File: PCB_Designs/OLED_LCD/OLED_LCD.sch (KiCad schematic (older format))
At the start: 25 parts, among them P1 CONN_01X10, P2 CONN_01X20, SW1 Rotary_Encoder_Switch, U1 MCP23017, U2 MCP23017, U3 CHERRY-MX

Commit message: s¨å
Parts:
- removed 0.1k1: 100, Resistors_SMD:R_0603_HandSoldering, symbol R
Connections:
- net LED+ is gone; now on net LCD_BACKLIGHT: P2.19 (P19)
- net RST#: no longer U1.18 (~RESET), U2.18 (~RESET)
- no-connect marks 19 -> 21
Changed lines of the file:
@@
 Text Label 4550 4350 0    60   ~ 0
 GND
-Text Label 5050 2550 0    60   ~ 0
-RST#
 Wire Wire Line
 	5050 3950 5150 3950
@@
 Text Label 7300 4000 2    60   ~ 0
 VEE
-Text Label 7300 4100 2    60   ~ 0
-LED+
 Text Label 7300 4200 2    60   ~ 0
 LED-
-$Comp
-L R 0.1k1
-U 1 1 58950747
-P 6000 4250
-F 0 "0.1k1" V 6080 4250 50  0000 C CNN
-F 1 "100" V 6000 4250 50  0000 C CNN
-F 2 "Resistors_SMD:R_0603_HandSoldering" V 5930 4250 50  0001 C CNN
-F 3 "" H 6000 4250 50  0000 C CNN
-	1    6000 4250
-	1    0    0    -1
-$EndComp
-Wire Wire Line
-	6000 4550 6000 4400
-Text Label 6000 4100 0    60   ~ 0
-LED+
-Text Label 6000 4550 0    60   ~ 0
-VCC5
 $Comp
 L GND #PWR03
@@
 Text Label 2500 3750 0    60   ~ 0
 SDA#
-Text Label 2500 2550 0    60   ~ 0
-RST#
 Text Label 2500 3050 0    60   ~ 0
 INTA
@@
 	1    0    0    -1
 $EndComp
+Text Label 7300 4100 2    60   ~ 0
+LCD_BACKLIGHT
+NoConn ~ 5050 2550
+NoConn ~ 2500 2550
 $EndSCHEMATC

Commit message: LCD123
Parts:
- P1: footprint Connectors:IDC_Header_Straight_10pins -> Connectors_Multicomp:Multicomp_MC9A22-1034_2x05x2.54mm_Angled
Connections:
- net GND: now also P1.4 (P4)
- net INTA: now also P1.10 (P10)
- net SCL#: now also P1.8 (P8)
- net SDA#: now also P1.6 (P6)
- net INTB: no longer names the net of U1.19 (INTB)
- no-connect marks 21 -> 19
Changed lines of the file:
@@
 Text Label 2500 3050 0    60   ~ 0
 INTA
-Text Label 2500 2950 0    60   ~ 0
-INTB
 Text Label 2000 4350 0    60   ~ 0
 GND
@@
 F 0 "P1" H 6000 1850 50  0000 C CNN
 F 1 "CONN_01X10" V 6100 1300 50  0000 C CNN
-F 2 "Connectors:IDC_Header_Straight_10pins" H 6000 1300 50  0001 C CNN
+F 2 "Connectors_Multicomp:Multicomp_MC9A22-1034_2x05x2.54mm_Angled" H 6000 1300 50  0001 C CNN
 F 3 "" H 6000 1300 50  0000 C CNN
 	1    6000 1300
@@
 Text Label 5800 1250 2    60   ~ 0
 SDA#
-Text Label 4850 1150 2    60   ~ 0
-RST#
 Text Label 6550 3150 2    60   ~ 0
 VCC5DISP
@@
 	5050 3750 5500 3750
 Connection ~ 2000 2350
-NoConn ~ 5800 1750
 NoConn ~ 1500 3950
 NoConn ~ 1500 4050
 NoConn ~ 1500 4150
 Connection ~ 2500 3050
-Connection ~ 2500 2950
 Text Label 5800 1650 2    60   ~ 0
 INTA
@@
 Text Label 5800 950  2    60   ~ 0
 LCD_BACKLIGHT
-NoConn ~ 5800 1150
-NoConn ~ 5800 1350
-NoConn ~ 5800 1550
 Text Label 4200 1450 2    60   ~ 0
 VCC5
@@
 NoConn ~ 5050 2550
 NoConn ~ 2500 2550
+NoConn ~ 2500 2950
+NoConn ~ 2800 2950
+Wire Wire Line
+	5800 1050 5800 1150
+Wire Wire Line
+	5800 1250 5800 1350
+Wire Wire Line
+	5800 1450 5800 1550
+Wire Wire Line
+	5800 1650 5800 1750
 $EndSCHEMATC

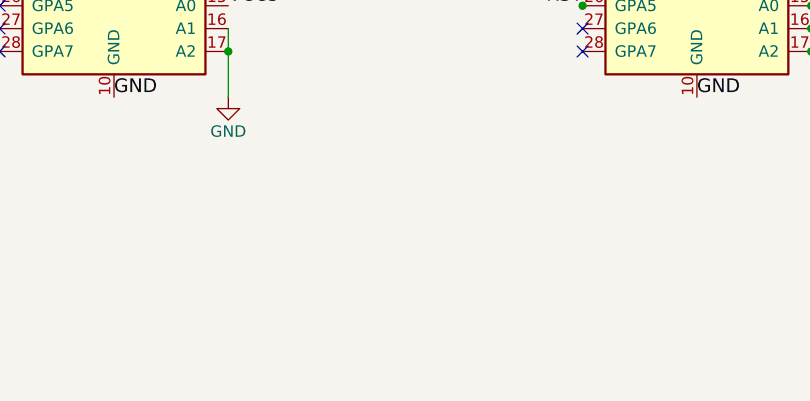
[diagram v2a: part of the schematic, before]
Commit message: Completed OLED_LCD_PCB v1.1
* Added Mountingholes.
* Added "Fatpads" for vias (were on some but not all earlier)
* Added bottom ground (Or etching will be a bitch)
* Added Edge cuts (105x65mm)
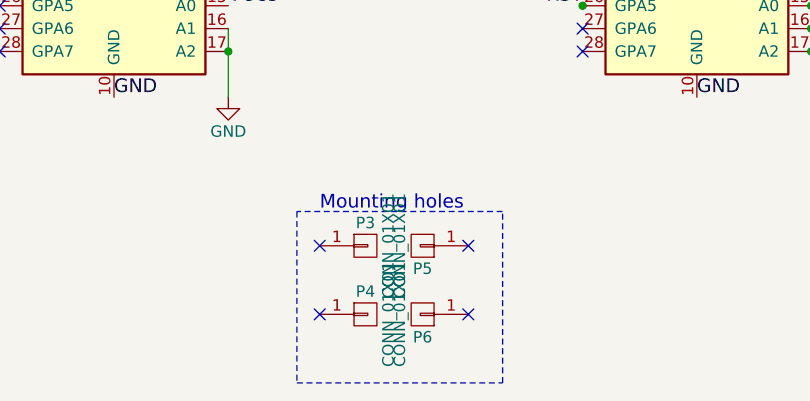
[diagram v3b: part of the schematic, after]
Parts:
- added P3, P4, P5, P6: CONN_01X01, Mounting_Holes:MountingHole_2.2mm_M2_DIN965_Pad, symbol CONN_01X01
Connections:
- no-connect marks 19 -> 23
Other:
- note added: "Mounting holes"
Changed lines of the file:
@@
 Wire Wire Line
 	5800 1650 5800 1750
+$Comp
+L CONN_01X01 P3
+U 1 1 58A4BCD7
+P 3100 5000
+F 0 "P3" H 3100 5100 50  0000 C CNN
+F 1 "CONN_01X01" V 3200 5000 50  0000 C CNN
+F 2 "Mounting_Holes:MountingHole_2.2mm_M2_DIN965_Pad" H 3100 5000 50  0001 C CNN
+F 3 "" H 3100 5000 50  0001 C CNN
+	1    3100 5000
+	1    0    0    -1
+$EndComp
+$Comp
+L CONN_01X01 P5
+U 1 1 58A4C0C0
+P 3350 5000
+F 0 "P5" H 3350 5100 50  0000 C CNN
+F 1 "CONN_01X01" V 3450 5000 50  0000 C CNN
+F 2 "Mounting_Holes:MountingHole_2.2mm_M2_DIN965_Pad" H 3350 5000 50  0001 C CNN
+F 3 "" H 3350 5000 50  0001 C CNN
+	1    3350 5000
+	-1   0    0    1
+$EndComp
+$Comp
+L CONN_01X01 P4
+U 1 1 58A4C14F
+P 3100 5300
+F 0 "P4" H 3100 5400 50  0000 C CNN
+F 1 "CONN_01X01" V 3200 5300 50  0000 C CNN
+F 2 "Mounting_Holes:MountingHole_2.2mm_M2_DIN965_Pad" H 3100 5300 50  0001 C CNN
+F 3 "" H 3100 5300 50  0001 C CNN
+	1    3100 5300
+	1    0    0    -1
+$EndComp
+$Comp
+L CONN_01X01 P6
+U 1 1 58A4C1C4
+P 3350 5300
+F 0 "P6" H 3350 5400 50  0000 C CNN
+F 1 "CONN_01X01" V 3450 5300 50  0000 C CNN
+F 2 "Mounting_Holes:MountingHole_2.2mm_M2_DIN965_Pad" H 3350 5300 50  0001 C CNN
+F 3 "" H 3350 5300 50  0001 C CNN
+	1    3350 5300
+	-1   0    0    1
+$EndComp
+Text Notes 2900 4850 0    60   ~ 0
+Mounting holes
+NoConn ~ 2900 5000
+NoConn ~ 2900 5300
+NoConn ~ 3550 5000
+NoConn ~ 3550 5300
+Wire Notes Line
+	3700 5600 3700 4850
+Wire Notes Line
+	3700 4850 2800 4850
+Wire Notes Line
+	2800 4850 2800 5600
+Wire Notes Line
+	2800 5600 3700 5600
 $EndSCHEMATC

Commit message: hej
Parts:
- removed 10k8: 10k, Potentiometers:Potentiometer_Trimmer-EVM3E, symbol POT
- removed P2: CONN_01X20, Pin_Headers:Pin_Header_Straight_1x20_Pitch2.54mm, symbol CONN_01X20
- added P2: CONN_01X16, Pin_Headers:Pin_Header_Straight_1x16_Pitch2.54mm, symbol CONN_01X16
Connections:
- net D0: now also P2.7 (P7)
- net D1: now also P2.8 (P8)
- net D2: now also P2.9 (P9)
- net D3: now also P2.10 (P10)
- net D4: now also P2.11 (P11)
- net D5: now also P2.12 (P12)
- net D6: now also P2.13 (P13)
- net D7: now also P2.14 (P14)
- net E: now also P2.6 (P6)
- net GND: now also P2.1 (P1), P2.16 (P16)
- net LCD_BACKLIGHT: now also P2.15 (P15)
- net RS: now also P2.4 (P4)
- net RW: now also P2.5 (P5)
- net VCC5: now also P2.2 (P2)
- net CS1: no longer names the net of U2.21 (GPA0)
- net CS2: no longer names the net of U2.22 (GPA1)
- net RST: no longer names the net of U2.26 (GPA5)
- no-connect marks 23 -> 27
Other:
- moved on the sheet: 100n3
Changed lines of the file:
@@
 Text Label 4050 3250 2    60   ~ 0
 D7
-$Comp
-L CONN_01X20 P2
-U 1 1 5894F9E5
-P 7500 3250
-F 0 "P2" H 7500 4300 50  0000 C CNN
-F 1 "CONN_01X20" V 7600 3250 50  0000 C CNN
-F 2 "Pin_Headers:Pin_Header_Straight_1x20_Pitch2.54mm" H 7500 3250 50  0001 C CNN
-F 3 "" H 7500 3250 50  0000 C CNN
-	1    7500 3250
-	1    0    0    -1
-$EndComp
 Text Label 4550 4350 0    60   ~ 0
 GND
@@
 L GND #PWR02
 U 1 1 5894FCE6
-P 6550 3800
-F 0 "#PWR02" H 6550 3550 50  0001 C CNN
-F 1 "GND" H 6550 3650 50  0000 C CNN
-F 2 "" H 6550 3800 50  0000 C CNN
-F 3 "" H 6550 3800 50  0000 C CNN
-	1    6550 3800
+P 6300 3250
+F 0 "#PWR02" H 6300 3000 50  0001 C CNN
+F 1 "GND" H 6300 3100 50  0000 C CNN
+F 2 "" H 6300 3250 50  0000 C CNN
+F 3 "" H 6300 3250 50  0000 C CNN
+	1    6300 3250
 	1    0    0    -1
 $EndComp
@@
 L C 100n3
 U 1 1 5894FD05
-P 6550 3500
-F 0 "100n3" H 6575 3600 50  0000 L CNN
-F 1 "100n" H 6575 3400 50  0000 L CNN
-F 2 "Capacitors_SMD:C_0603_HandSoldering" H 6588 3350 50  0001 C CNN
-F 3 "" H 6550 3500 50  0000 C CNN
-	1    6550 3500
-	1    0    0    -1
-$EndComp
-Wire Wire Line
-	6550 3800 6550 3650
-Text Label 6550 3350 0    60   ~ 0
+P 6300 2950
+F 0 "100n3" H 6325 3050 50  0000 L CNN
+F 1 "100n" H 6325 2850 50  0000 L CNN
+F 2 "Capacitors_SMD:C_0603_HandSoldering" H 6338 2800 50  0001 C CNN
+F 3 "" H 6300 2950 50  0000 C CNN
+	1    6300 2950
+	1    0    0    -1
+$EndComp
+Wire Wire Line
+	6300 3250 6300 3100
+Text Label 6300 2800 0    60   ~ 0
 VCC5
 Text Label 5050 3650 0    60   ~ 0
@@
 Text Label 5050 3750 0    60   ~ 0
 SDA#
-Text Label 4050 3450 2    60   ~ 0
-CS1
-Text Label 4050 3550 2    60   ~ 0
-CS2
 Text Label 4050 3650 2    60   ~ 0
 RS
@@
 Text Label 4050 3850 2    60   ~ 0
 E
-Text Label 4050 3950 2    60   ~ 0
-RST
 Text Label 7300 2300 2    60   ~ 0
-CS1
+GND
 Text Label 7300 2400 2    60   ~ 0
-CS2
-Text Label 7300 2500 2    60   ~ 0
-GND
+VCC5DISP
 Text Label 7300 2600 2    60   ~ 0
-VCC5DISP
+RS
 Text Label 7300 2700 2    60   ~ 0
-V0
+RW
 Text Label 7300 2800 2    60   ~ 0
-RS
+E
 Text Label 7300 2900 2    60   ~ 0
-RW
+D0
 Text Label 7300 3000 2    60   ~ 0
-E
+D1
 Text Label 7300 3100 2    60   ~ 0
-D0
+D2
 Text Label 7300 3200 2    60   ~ 0
-D1
+D3
 Text Label 7300 3300 2    60   ~ 0
-D2
+D4
 Text Label 7300 3400 2    60   ~ 0
-D3
+D5
 Text Label 7300 3500 2    60   ~ 0
-D4
+D6
 Text Label 7300 3600 2    60   ~ 0
-D5
-Text Label 7300 3700 2    60   ~ 0
-D6
+D7
 Text Label 7300 3800 2    60   ~ 0
-D7
-Text Label 7300 3900 2    60   ~ 0
-RST
-Text Label 7300 4000 2    60   ~ 0
-VEE
-Text Label 7300 4200 2    60   ~ 0
 LED-
 $Comp
@@
 L GND #PWR04
 U 1 1 58950905
-P 7150 4350
-F 0 "#PWR04" H 7150 4100 50  0001 C CNN
-F 1 "GND" H 7150 4200 50  0000 C CNN
-F 2 "" H 7150 4350 50  0000 C CNN
-F 3 "" H 7150 4350 50  0000 C CNN
-	1    7150 4350
-	1    0    0    -1
-$EndComp
-Wire Wire Line
-	7300 4200 7150 4200
-Wire Wire Line
-	7150 4200 7150 4350
-$Comp
-L POT 10k8
-U 1 1 58950B2C
-P 6150 2600
-F 0 "10k8" V 5975 2600 50  0000 C CNN
-F 1 "10k" V 6050 2600 50  0000 C CNN
-F 2 "Potentiometers:Potentiometer_Trimmer-EVM3E" H 6150 2600 50  0001 C CNN
-F 3 "" H 6150 2600 50  0000 C CNN
-	1    6150 2600
-	0    1    1    0
-$EndComp
-Text Label 6300 2600 0    60   ~ 0
-VEE
-Text Label 6000 2600 2    60   ~ 0
-GND
-Text Label 6150 2750 0    60   ~ 0
-V0
+P 7100 3900
+F 0 "#PWR04" H 7100 3650 50  0001 C CNN
+F 1 "GND" H 7100 3750 50  0000 C CNN
+F 2 "" H 7100 3900 50  0000 C CNN
+F 3 "" H 7100 3900 50  0000 C CNN
+	1    7100 3900
+	1    0    0    -1
+$EndComp
 $Comp
 L MCP23017 U1
@@
 Wire Wire Line
 	2700 1100 2700 1250
-Connection ~ 6550 3650
+Connection ~ 6300 3100
 Connection ~ 5050 3950
 Connection ~ 5050 4050
@@
 Connection ~ 4050 2650
 Connection ~ 4050 2550
-Connection ~ 4050 3450
-Connection ~ 4050 3550
 Connection ~ 4050 3650
 Connection ~ 4050 3750
 Connection ~ 4050 3850
-Connection ~ 4050 3950
 NoConn ~ 4050 4050
 NoConn ~ 4050 4150
@@
 Text Label 5800 1250 2    60   ~ 0
 SDA#
-Text Label 6550 3150 2    60   ~ 0
+Text Label 6300 2600 2    60   ~ 0
 VCC5DISP
 Wire Wire Line
-	6550 3150 6550 3350
-Connection ~ 6550 3350
+	6300 2600 6300 2800
+Connection ~ 6300 2800
 $Comp
 L R 10k6
@@
 	1    0    0    -1
 $EndComp
-Text Label 7300 4100 2    60   ~ 0
+Text Label 7300 3700 2    60   ~ 0
 LCD_BACKLIGHT
 NoConn ~ 5050 2550
@@
 Wire Notes Line
 	2800 5600 3700 5600
+NoConn ~ 7300 2500
+Wire Wire Line
+	7100 3900 7100 3800
+Wire Wire Line
+	7100 3800 7300 3800
+Connection ~ 7300 3800
+$Comp
+L CONN_01X16 P2
+U 1 1 58B162AE
+P 7500 3050
+F 0 "P2" H 7500 3900 50  0000 C CNN
+F 1 "CONN_01X16" V 7600 3050 50  0000 C CNN
+F 2 "Pin_Headers:Pin_Header_Straight_1x16_Pitch2.54mm" H 7500 3050 50  0001 C CNN
+F 3 "" H 7500 3050 50  0000 C CNN
+	1    7500 3050
+	1    0    0    -1
+$EndComp
+NoConn ~ 4050 3450
+NoConn ~ 4050 3550
+NoConn ~ 4050 3950
 $EndSCHEMATC

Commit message: LCD Reset -> 5V
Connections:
- net VCC5: now also U1.18 (~RESET)
- no-connect marks 27 -> 25
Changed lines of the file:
@@
 LCD_BACKLIGHT
 NoConn ~ 5050 2550
-NoConn ~ 2500 2550
 NoConn ~ 2500 2950
-NoConn ~ 2800 2950
 Wire Wire Line
 	5800 1050 5800 1150
@@
 NoConn ~ 4050 3550
 NoConn ~ 4050 3950
+Text Label 2500 2550 0    60   ~ 0
+VCC5
+$Comp
+L PWR_FLAG #FLG011
+U 1 1 58B2ED0B
+P 6300 2800
+F 0 "#FLG011" H 6300 2875 50  0001 C CNN
+F 1 "PWR_FLAG" H 6300 2950 50  0000 C CNN
+F 2 "" H 6300 2800 50  0001 C CNN
+F 3 "" H 6300 2800 50  0001 C CNN
+	1    6300 2800
+	0    -1   -1   0
+$EndComp
+$Comp
+L PWR_FLAG #FLG012
+U 1 1 58B2EF20
+P 6300 3100
+F 0 "#FLG012" H 6300 3175 50  0001 C CNN
+F 1 "PWR_FLAG" H 6300 3250 50  0000 C CNN
+F 2 "" H 6300 3100 50  0001 C CNN
+F 3 "" H 6300 3100 50  0001 C CNN
+	1    6300 3100
+	0    -1   -1   0
+$EndComp
 $EndSCHEMATC

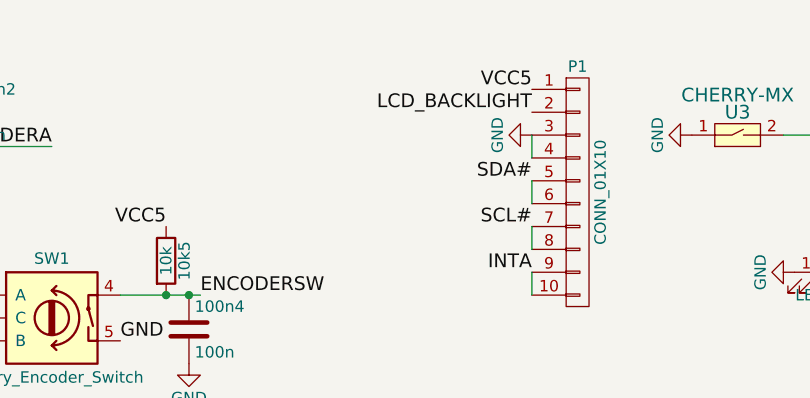
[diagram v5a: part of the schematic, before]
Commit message: Oled and photomasks
* Added 1k Serie resistance to backlight in Oled LCD.
* Created the photomasks for Buttons and Sliders.
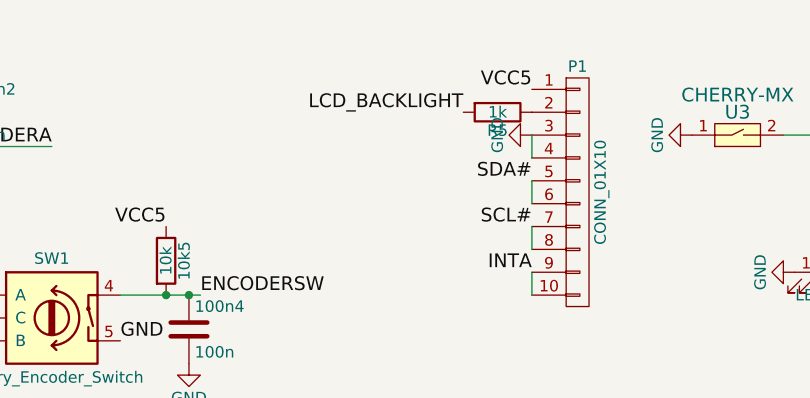
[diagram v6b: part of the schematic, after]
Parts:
- added R5: 1k, Resistors_SMD:R_0603_HandSoldering, symbol R
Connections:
- net LCD_BACKLIGHT: now also R5.2; no longer P1.2 (P2)
- new net: P1.2 (P2), R5.1
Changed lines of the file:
@@
 Connection ~ 5150 4150
 $Comp
-L GND #PWR01
+L GND #PWR3
 U 1 1 5894FC28
 P 5150 4300
-F 0 "#PWR01" H 5150 4050 50  0001 C CNN
+F 0 "#PWR3" H 5150 4050 50  0001 C CNN
 F 1 "GND" H 5150 4150 50  0000 C CNN
 F 2 "" H 5150 4300 50  0000 C CNN
@@
 $EndComp
 $Comp
-L GND #PWR02
+L GND #PWR5
 U 1 1 5894FCE6
 P 6300 3250
-F 0 "#PWR02" H 6300 3000 50  0001 C CNN
+F 0 "#PWR5" H 6300 3000 50  0001 C CNN
 F 1 "GND" H 6300 3100 50  0000 C CNN
 F 2 "" H 6300 3250 50  0000 C CNN
@@
 LED-
 $Comp
-L GND #PWR03
+L GND #PWR7
 U 1 1 589508C9
 P 6600 4350
-F 0 "#PWR03" H 6600 4100 50  0001 C CNN
+F 0 "#PWR7" H 6600 4100 50  0001 C CNN
 F 1 "GND" H 6600 4200 50  0000 C CNN
 F 2 "" H 6600 4350 50  0000 C CNN
@@
 GND
 $Comp
-L GND #PWR04
+L GND #PWR9
 U 1 1 58950905
 P 7100 3900
-F 0 "#PWR04" H 7100 3650 50  0001 C CNN
+F 0 "#PWR9" H 7100 3650 50  0001 C CNN
 F 1 "GND" H 7100 3750 50  0000 C CNN
 F 2 "" H 7100 3900 50  0000 C CNN
@@
 	2500 4050 2500 4350
 $Comp
-L GND #PWR05
+L GND #PWR1
 U 1 1 58951194
 P 2500 4350
-F 0 "#PWR05" H 2500 4100 50  0001 C CNN
+F 0 "#PWR1" H 2500 4100 50  0001 C CNN
 F 1 "GND" H 2500 4200 50  0000 C CNN
 F 2 "" H 2500 4350 50  0000 C CNN
@@
 Connection ~ 4300 1750
 $Comp
-L GND #PWR06
+L GND #PWR2
 U 1 1 58A0D2DB
 P 4300 2050
-F 0 "#PWR06" H 4300 1800 50  0001 C CNN
+F 0 "#PWR2" H 4300 1800 50  0001 C CNN
 F 1 "GND" H 4300 1900 50  0000 C CNN
 F 2 "" H 4300 2050 50  0000 C CNN
@@
 BUTTON_2
 $Comp
-L GND #PWR07
+L GND #PWR8
 U 1 1 58A0E8E0
 P 6950 1650
-F 0 "#PWR07" H 6950 1400 50  0001 C CNN
+F 0 "#PWR8" H 6950 1400 50  0001 C CNN
 F 1 "GND" H 6950 1500 50  0000 C CNN
 F 2 "" H 6950 1650 50  0000 C CNN
@@
 $EndComp
 $Comp
-L GND #PWR08
+L GND #PWR4
 U 1 1 58A0F70D
 P 5800 1050
-F 0 "#PWR08" H 5800 800 50  0001 C CNN
+F 0 "#PWR4" H 5800 800 50  0001 C CNN
 F 1 "GND" H 5800 900 50  0000 C CNN
 F 2 "" H 5800 1050 50  0000 C CNN
@@
 	0    1    1    0
 $EndComp
-Text Label 5800 950  2    60   ~ 0
+Text Label 5500 950  2    60   ~ 0
 LCD_BACKLIGHT
 Text Label 4200 1450 2    60   ~ 0
@@
 VCC5
 $Comp
-L GND #PWR09
+L GND #PWR6
 U 1 1 58A10FD4
 P 6500 1050
-F 0 "#PWR09" H 6500 800 50  0001 C CNN
+F 0 "#PWR6" H 6500 800 50  0001 C CNN
 F 1 "GND" H 6500 900 50  0000 C CNN
 F 2 "" H 6500 1050 50  0000 C CNN
@@
 $EndComp
 $Comp
-L GND #PWR010
+L GND #PWR10
 U 1 1 58A1101A
 P 7550 1350
-F 0 "#PWR010" H 7550 1100 50  0001 C CNN
+F 0 "#PWR10" H 7550 1100 50  0001 C CNN
 F 1 "GND" H 7550 1200 50  0000 C CNN
 F 2 "" H 7550 1350 50  0000 C CNN
@@
 VCC5
 $Comp
-L PWR_FLAG #FLG011
+L PWR_FLAG #FLG1
 U 1 1 58B2ED0B
 P 6300 2800
-F 0 "#FLG011" H 6300 2875 50  0001 C CNN
+F 0 "#FLG1" H 6300 2875 50  0001 C CNN
 F 1 "PWR_FLAG" H 6300 2950 50  0000 C CNN
 F 2 "" H 6300 2800 50  0001 C CNN
@@
 $EndComp
 $Comp
-L PWR_FLAG #FLG012
+L PWR_FLAG #FLG2
 U 1 1 58B2EF20
 P 6300 3100
-F 0 "#FLG012" H 6300 3175 50  0001 C CNN
+F 0 "#FLG2" H 6300 3175 50  0001 C CNN
 F 1 "PWR_FLAG" H 6300 3250 50  0000 C CNN
 F 2 "" H 6300 3100 50  0001 C CNN
@@
 	0    -1   -1   0
 $EndComp
+$Comp
+L R R5
+U 1 1 58B42B31
+P 5650 950
+F 0 "R5" V 5730 950 50  0000 C CNN
+F 1 "1k" V 5650 950 50  0000 C CNN
+F 2 "Resistors_SMD:R_0603_HandSoldering" V 5580 950 50  0001 C CNN
+F 3 "" H 5650 950 50  0001 C CNN
+	1    5650 950
+	0    1    1    0
+$EndComp
 $EndSCHEMATC
